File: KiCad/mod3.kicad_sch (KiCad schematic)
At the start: 44 parts, among them M5 Fan_4pin, M6 Fan_4pin

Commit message: Fix some diodes and resistors
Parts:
- D11, D12: value 1N5819WS -> B0520W
- R145: value R_Small -> 21.5k
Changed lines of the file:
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@@
 			)
 		)
-		(property "Value" "1N5819WS"
+		(property "Value" "B0520W"
 			(at 382.27 46.99 90)
 			(effects
@@
 			)
 		)
-		(property "Value" "1N5819WS"
+		(property "Value" "B0520W"
 			(at 327.66 46.99 90)
 			(effects
@@
 			)
 		)
-		(property "Value" "R_Small"
+		(property "Value" "21.5k"
 			(at 377.19 60.9599 0)
 			(effects

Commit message: Add external BIOS flash
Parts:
- added C325: 100nF, symbol Device:C_Small
- added R202, R203, R204: 10k, symbol Device:R_Small
- added U13: W25Q128JVS, Package_SO:SOIC-8_5.3x5.3mm_P1.27mm, symbol Memory_Flash:W25Q128JVS
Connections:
- net +3V3: now also C325.1, R202.1, R204.1, U13.8 (VCC)
- net GND: now also C325.2, R203.2, U13.4 (GND)
- net at A3.133 (~{BIOS_SEL}): now also R203.1
- net at A3.153 (SPI_IO3): now also R202.2, U13.7 (~{HOLD}/~{RESET}/IO_{3})
- net at A3.155 (SPI_CLK): now also U13.6 (CLK)
- net at A3.159 (SPI_MOSI/SPI_IO0): now also U13.5 (DI/IO_{0})
- net at A3.161 (SPI_IO2): now also R204.2, U13.3 (~{WP}/IO_{2})
- net at A3.163 (SPI_MISO/SPI_IO1): now also U13.2 (DO/IO_{1})
- net at A3.165 (~{SPI_CS}): now also U13.1 (~{CS})
- no-connect marks 5 -> 6

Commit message: Remove 0.95V Power Supply, Replace 3.3V Standby Power Supply
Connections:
- no-connect marks 6 -> 111

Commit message: Work though ERC errors
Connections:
- net ETH.SMBCLK: now reaches A3.106 (SMB_CLK)
- net ETH.SMBDAT: now reaches A3.108 (SMB_DATA)
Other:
- moved on the sheet: R16
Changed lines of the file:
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@@
 	)
 	(junction
+		(at 275.59 69.85)
+		(diameter 0)
+		(color 0 0 0 0)
+	)
+	(junction
 		(at 392.43 49.53)
 		(diameter 0)
@@
 	)
 	(no_connect
-		(at 313.69 153.67)
-	)
-	(no_connect
 		(at 232.41 318.77)
 	)
@@
 	)
 	(no_connect
+		(at 232.41 87.63)
+	)
+	(no_connect
 		(at 232.41 125.73)
 	)
@@
 	)
 	(no_connect
+		(at 313.69 151.13)
+	)
+	(no_connect
 		(at 232.41 280.67)
 	)
@@
 	)
 	(no_connect
-		(at 232.41 325.12)
+		(at 232.41 326.39)
 	)
 	(no_connect
@@
 	)
 	(no_connect
+		(at 232.41 90.17)
+	)
+	(no_connect
 		(at 232.41 266.7)
 	)
@@
 	)
 	(no_connect
-		(at 313.69 214.63)
-	)
-	(no_connect
 		(at 313.69 177.8)
 	)
@@
 	)
 	(no_connect
-		(at 313.69 212.09)
-	)
-	(no_connect
 		(at 313.69 172.72)
 	)
@@
 	)
 	(bus_entry
+		(at 330.2 212.09)
+		(size -2.54 2.54)
+		(stroke
+			(width 0)
+			(type default)
+		)
+	)
+	(bus_entry
 		(at 372.11 109.22)
 		(size -2.54 2.54)
@@
 	)
 	(bus_entry
+		(at 330.2 209.55)
+		(size -2.54 2.54)
+		(stroke
+			(width 0)
+			(type default)
+		)
+	)
+	(bus_entry
 		(at 199.39 107.95)
 		(size 2.54 2.54)
@@
 	(wire
 		(pts
-			(xy 275.59 62.23) (xy 275.59 64.77)
+			(xy 275.59 62.23) (xy 275.59 63.5)
 		)
 		(stroke
@@
 	(wire
 		(pts
+			(xy 313.69 212.09) (xy 327.66 212.09)
+		)
+		(stroke
+			(width 0)
+			(type default)
+		)
+	)
+	(wire
+		(pts
 			(xy 226.06 300.99) (xy 232.41 300.99)
 		)
@@
 	(wire
 		(pts
+			(xy 281.94 69.85) (xy 275.59 69.85)
+		)
+		(stroke
+			(width 0)
+			(type default)
+		)
+	)
+	(wire
+		(pts
 			(xy 323.85 267.97) (xy 323.85 252.73)
 		)
@@
 	(bus
 		(pts
+			(xy 330.2 209.55) (xy 330.2 212.09)
+		)
+		(stroke
+			(width 0)
+			(type default)
+		)
+	)
+	(bus
+		(pts
 			(xy 336.55 96.52) (xy 336.55 99.06)
 		)
@@
 		)
 	)
+	(bus
+		(pts
+			(xy 330.2 208.28) (xy 330.2 209.55)
+		)
+		(stroke
+			(width 0)
+			(type default)
+		)
+	)
 	(wire
 		(pts
@@
 	(wire
 		(pts
+			(xy 281.94 67.31) (xy 281.94 69.85)
+		)
+		(stroke
+			(width 0)
+			(type default)
+		)
+	)
+	(wire
+		(pts
 			(xy 201.93 102.87) (xy 232.41 102.87)
 		)
@@
 	(wire
 		(pts
-			(xy 275.59 69.85) (xy 275.59 72.39)
+			(xy 275.59 68.58) (xy 275.59 69.85)
 		)
 		(stroke
@@
 	(wire
 		(pts
+			(xy 313.69 214.63) (xy 327.66 214.63)
+		)
+		(stroke
+			(width 0)
+			(type default)
+		)
+	)
+	(wire
+		(pts
 			(xy 201.93 194.31) (xy 232.41 194.31)
 		)
@@
 		)
 	)
+	(wire
+		(pts
+			(xy 275.59 69.85) (xy 275.59 72.39)
+		)
+		(stroke
+			(width 0)
+			(type default)
+		)
+	)
 	(bus
 		(pts
@@
 		)
 	)
+	(label "ETH.SMBDAT"
+		(at 314.96 212.09 0)
+		(effects
+			(font
+				(size 1.27 1.27)
+			)
+			(justify left bottom)
+		)
+	)
 	(label "M2_EKEY{PCIE}"
 		(at 372.11 87.63 0)
@@
 		)
 	)
+	(label "ETH{PCIE}"
+		(at 330.2 208.28 0)
+		(effects
+			(font
+				(size 1.27 1.27)
+			)
+			(justify left bottom)
+		)
+	)
 	(label "M2_EKEY.Tx0+"
 		(at 203.2 115.57 0)
@@
 		)
 	)
+	(label "ETH.SMBCLK"
+		(at 314.96 214.63 0)
+		(effects
+			(font
+				(size 1.27 1.27)
+			)
+			(justify left bottom)
+		)
+	)
 	(label "ETH{PCIE}"
 		(at 336.55 87.63 0)
@@
 	(symbol
 		(lib_id "Device:R_Small")
-		(at 275.59 67.31 0)
+		(at 275.59 66.04 0)
 		(unit 1)
 		(exclude_from_sim no)
@@
 		(fields_autoplaced yes)
 		(property "Reference" "R16"
-			(at 278.13 66.0399 0)
+			(at 278.13 64.7699 0)
 			(effects
 				(font
@@
 		)
 		(property "Value" "1k"
-			(at 278.13 68.5799 0)
+			(at 278.13 67.3099 0)
 			(effects
 				(font
@@
 		)
 		(property "Footprint" ""
-			(at 275.59 67.31 0)
+			(at 275.59 66.04 0)
 			(effects
 				(font
@@
 		)
 		(property "Datasheet" "~"
-			(at 275.59 67.31 0)
+			(at 275.59 66.04 0)
 			(effects
 				(font
@@
 		)
 		(property "Description" "Resistor, small symbol"
-			(at 275.59 67.31 0)
+			(at 275.59 66.04 0)
 			(effects
 				(font
@@
 					(unit 1)
 				)
+			)
+		)
+	)
+	(symbol
+		(lib_id "power:PWR_FLAG")
+		(at 281.94 67.31 0)
+		(unit 1)
+		(exclude_from_sim no)
+		(in_bom yes)
+		(on_board yes)
+		(dnp no)
+		(fields_autoplaced yes)
+		(property "Reference" "#FLG013"
+			(at 281.94 65.405 0)
+			(effects
+				(font
+					(size 1.27 1.27)
+				)
+				(hide yes)
+			)
+		)
+		(property "Value" "PWR_FLAG"
+			(at 281.94 62.23 0)
+			(effects
+				(font
+					(size 1.27 1.27)
+				)
+			)
+		)
+		(property "Footprint" ""
+			(at 281.94 67.31 0)
+			(effects
+				(font
+					(size 1.27 1.27)
+				)
+				(hide yes)
+			)
+		)
+		(property "Datasheet" "~"
+			(at 281.94 67.31 0)
+			(effects
+				(font
+					(size 1.27 1.27)
+				)
+				(hide yes)
+			)
+		)
+		(property "Description" "Special symbol for telling ERC where power comes from"
+			(at 281.94 67.31 0)
+			(effects
+				(font
+					(size 1.27 1.27)
+				)
+				(hide yes)
+			)
+		)
+		(pin "1"
+		)
+		(instances
+			(project "LattePandaMuCluster"
+				(path "/49abeb3a-c598-45a3-ba6b-595eb04f17a8/8efff908-26ae-4c7c-94bd-59dcef311495"
+					(reference "#FLG013")
+					(unit 1)
+				)

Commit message: Re-annotate components
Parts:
- C75: renamed from C69; value 100nF -> 220nF
- C76: renamed from C70; value 100nF -> 220nF
- renumbered C51 to C57, C52 to C58, C53 to C59, C54 to C60, C55 to C61, C56 to C62, C57 to C63, C58 to C64, C59 to C65, C60 to C66, C61 to C67, C62 to C68, C63 to C69, C64 to C70, C65 to C71, C66 to C72, C67 to C73, C68 to C74, C292 to C77, C325 to C78, C293 to C79, D24 to D10, D19 to D9, R165 to R45, R13 to R46, R14 to R47, R15 to R48, R16 to R49, R202 to R50, R203 to R51, R17 to R52, R18 to R53, R204 to R54, R142 to R55, R143 to R56, R178 to R57, R144 to R58, R145 to R59, R146 to R60, R147 to R61, R148 to R62, U13 to U3

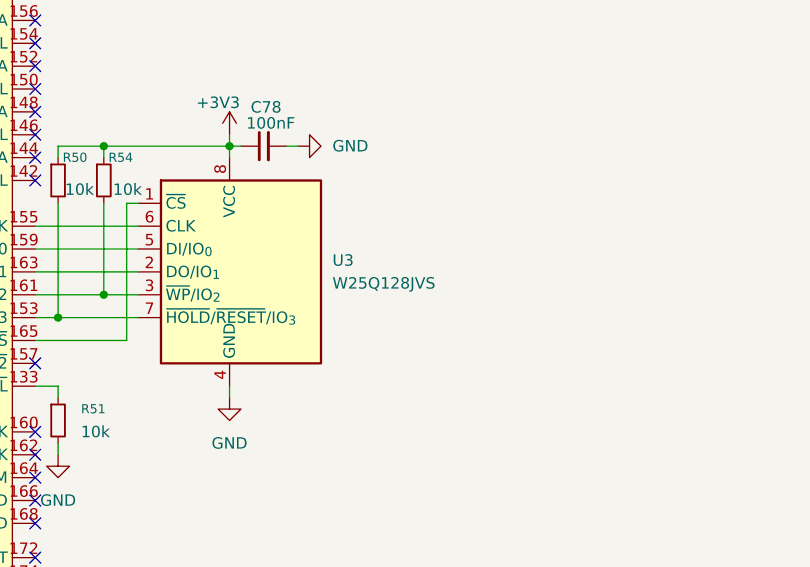
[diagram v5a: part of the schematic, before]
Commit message: Add TVS diodes for ESD protection
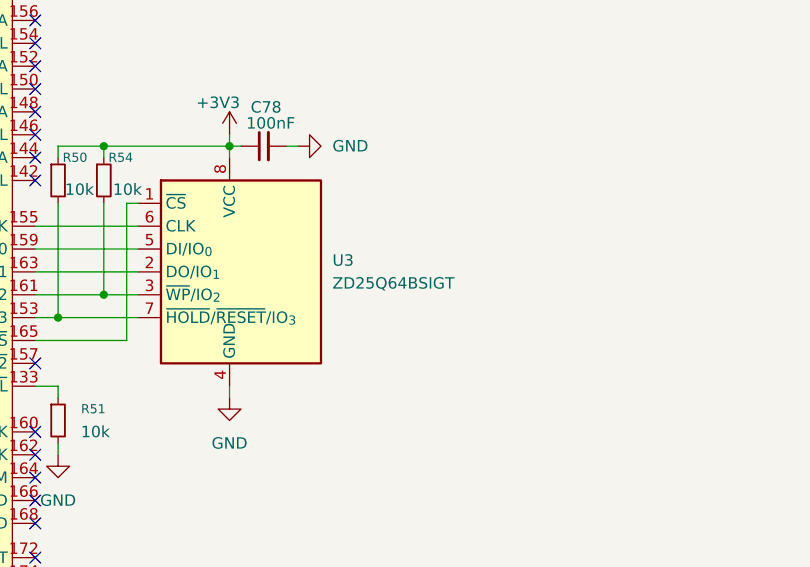
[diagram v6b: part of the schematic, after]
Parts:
- U3: value W25Q128JVS -> ZD25Q64BSIGT
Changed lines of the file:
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@@
 			)
 		)
-		(property "Value" "W25Q128JVS"
+		(property "Value" "ZD25Q64BSIGT"
 			(at 346.71 261.6199 0)
 			(effects

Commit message: Add more footprints
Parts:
- A3: footprint Module_LattePanda:LattePanda_Module_H8.0mm_Horizontal -> 124B-150A02:ATTEND_124B-150A02
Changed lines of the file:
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@@
 			)
 		)
-		(property "Footprint" "Module_LattePanda:LattePanda_Module_H8.0mm_Horizontal"
+		(property "Footprint" "124B-150A02:ATTEND_124B-150A02"
 			(at 273.05 196.85 0)
 			(effects

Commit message: Add more footprints
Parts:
- C57, C58, C59, C60, C61, C62, C63, C64, C65, C66, C67, C68, C69, C70, C71, C72, C73, C74, C75, C76, C77, C78, C79: footprint (none) -> Capacitor_SMD:C_0603_1608Metric
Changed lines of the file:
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@@
 			)
 		)
-		(property "Footprint" ""
+		(property "Footprint" "Capacitor_SMD:C_0603_1608Metric"
 			(at 223.52 168.91 0)
 			(effects
@@
 			)
 		)
-		(property "Footprint" ""
+		(property "Footprint" "Capacitor_SMD:C_0603_1608Metric"
 			(at 223.52 158.75 0)
 			(effects
@@
 			)
 		)
-		(property "Footprint" ""
+		(property "Footprint" "Capacitor_SMD:C_0603_1608Metric"
 			(at 223.52 163.83 0)
 			(effects
@@
 			)
 		)
-		(property "Footprint" ""
+		(property "Footprint" "Capacitor_SMD:C_0603_1608Metric"
 			(at 223.52 173.99 0)
 			(effects
@@
 			)
 		)
-		(property "Footprint" ""
+		(property "Footprint" "Capacitor_SMD:C_0603_1608Metric"
 			(at 320.04 44.45 0)
 			(effects
@@
 			)
 		)
-		(property "Footprint" ""
+		(property "Footprint" "Capacitor_SMD:C_0603_1608Metric"
 			(at 223.52 140.97 0)
 			(effects
@@
 			)
 		)
-		(property "Footprint" ""
+		(property "Footprint" "Capacitor_SMD:C_0603_1608Metric"
 			(at 223.52 138.43 0)
 			(effects
@@
 			)
 		)
-		(property "Footprint" ""
+		(property "Footprint" "Capacitor_SMD:C_0603_1608Metric"
 			(at 223.52 115.57 0)
 			(effects
@@
 			)
 		)
-		(property "Footprint" ""
+		(property "Footprint" "Capacitor_SMD:C_0603_1608Metric"
 			(at 223.52 118.11 0)
 			(effects
@@
 			)
 		)
-		(property "Footprint" ""
+		(property "Footprint" "Capacitor_SMD:C_0603_1608Metric"
 			(at 223.52 107.95 0)
 			(effects
@@
 			)
 		)
-		(property "Footprint" ""
+		(property "Footprint" "Capacitor_SMD:C_0603_1608Metric"
 			(at 370.84 44.45 0)
 			(effects
@@
 			)
 		)
-		(property "Footprint" ""
+		(property "Footprint" "Capacitor_SMD:C_0603_1608Metric"
 			(at 223.52 95.25 0)
 			(effects
@@
 			)
 		)
-		(property "Footprint" ""
+		(property "Footprint" "Capacitor_SMD:C_0603_1608Metric"
 			(at 223.52 151.13 0)
 			(effects
@@
 			)
 		)
-		(property "Footprint" ""
+		(property "Footprint" "Capacitor_SMD:C_0603_1608Metric"
 			(at 223.52 171.45 0)
 			(effects
@@
 			)
 		)
-		(property "Footprint" ""
+		(property "Footprint" "Capacitor_SMD:C_0603_1608Metric"
 			(at 223.52 184.15 0)
 			(effects
@@
 			)
 		)
-		(property "Footprint" ""
+		(property "Footprint" "Capacitor_SMD:C_0603_1608Metric"
 			(at 223.52 161.29 0)
 			(effects
@@
 			)
 		)
-		(property "Footprint" ""
+		(property "Footprint" "Capacitor_SMD:C_0603_1608Metric"
 			(at 223.52 166.37 0)
 			(effects
@@
 			)
 		)
-		(property "Footprint" ""
+		(property "Footprint" "Capacitor_SMD:C_0603_1608Metric"
 			(at 223.52 105.41 0)
 			(effects
@@
 			)
 		)
-		(property "Footprint" ""
+		(property "Footprint" "Capacitor_SMD:C_0603_1608Metric"
 			(at 223.52 148.59 0)
 			(effects
@@
 			)
 		)
-		(property "Footprint" ""
+		(property "Footprint" "Capacitor_SMD:C_0603_1608Metric"
 			(at 339.09 246.38 0)
 			(effects
@@
 			)
 		)
-		(property "Footprint" ""
+		(property "Footprint" "Capacitor_SMD:C_0603_1608Metric"
 			(at 223.52 176.53 0)
 			(effects
@@
 			)
 		)
-		(property "Footprint" ""
+		(property "Footprint" "Capacitor_SMD:C_0603_1608Metric"
 			(at 223.52 97.79 0)
 			(effects
@@
 			)
 		)
-		(property "Footprint" ""
+		(property "Footprint" "Capacitor_SMD:C_0603_1608Metric"
 			(at 223.52 181.61 0)
 			(effects
